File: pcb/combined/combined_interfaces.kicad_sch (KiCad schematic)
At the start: 19 parts, among them J5 CAN BUS, J6 FLOW HALL, J8 BOILER SSR, Q5 AO3401A, Q6 2N7002, U4 TJA1051T/3, U5 TMP102AIDRLR

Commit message: Draw the combined v2 schematic: 24 V buck and isolated gear pump interface
The pump dimmer and the zero-cross detector leave the board; the 230 V
valve channel stays. J7 brings 24 V from the pump supply to an
LMR33630A buck (5.02 V, enable at 18.4 V, off at 16.9 V), and J1 now sends
5 V to the screen. Two EL817C keep the pump's signal wires on their
isolated side: U8 turns the 1 kHz PWM on GPIO1 into a filtered setpoint
from the pump's own 5 V, U9 brings the tachometer back to GPIO3. DIM and
ZC become PUMP_SPEED and PUMP_TACHO.

The XIAO 5V pin is its USB VBUS with no diode; no diode is added either,
so USB is never plugged in with the XIAO on the board. New parts take new
references, so that no low-voltage net inherits a stale Mains netclass
pattern; those patterns and the pump and zero-cross DRC rules are gone.

F1 drops to 0.5 A, now that it protects the valve alone, and the AC
tracks to 1 mm. J3 is reversed so that its N faces N on J2. The HT396R
outline follows the Kefa drawing, and J8 becomes an HT396V header whose
screw plug takes the 0.75 mm² wires to the boiler SSR.

The board has been updated from the schematic; placement and routing are
still in progress.

Co-Authored-By: Claude Opus 5.5 <noreply@anthropic.com>
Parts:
- J8: footprint Connector_JST:JST_XH_B2B-XH-A_1x02_P2.50mm_Vertical -> Combined_Local:CONN-TH_P3.96_HT396V-3.96-2P; LCSC C158012 -> C577788; MPN B2B-XH-A(LF)(SN) -> HT396V-3.96-2P
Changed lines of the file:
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@@
 			)
 		)
-		(property "Footprint" "Connector_JST:JST_XH_B2B-XH-A_1x02_P2.50mm_Vertical"
+		(property "Footprint" "Combined_Local:CONN-TH_P3.96_HT396V-3.96-2P"
 			(at 288.29 242.57 0)
 			(hide yes)
@@
 			)
 		)
-		(property "Description" "Generic connector, single row, 01x02, script generated (kicad-library-utils/schlib/autogen/connector/)"
+		(property "Description" "Kefa HT396V vertical header; mating plug HT396K-3.96-2P (C577777, screw, up to 1.5 mm2) takes the 0.75 mm2 wires to the boiler SSR: 1 SSR (-), 2 SSR (+)"
 			(at 288.29 242.57 0)
 			(hide yes)
@@
 			)
 		)
-		(property "MPN" "B2B-XH-A(LF)(SN)"
+		(property "MPN" "HT396V-3.96-2P"
 			(at 288.29 242.57 0)
 			(hide yes)
@@
 			)
 		)
-		(property "LCSC" "C158012"
+		(property "LCSC" "C577788"
 			(at 288.29 242.57 0)
 			(hide yes)

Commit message: Move combined to basic passives, M2 holes and an HT3.96 flow connector
- Mounting holes H1 to H6 become M2 (2.2 mm NPTH) and move on the board;
  the AC wing narrows to 35 mm.
- Nine extended passives become JLCPCB basic parts: R3 150, R5/R6
  300 + 300, R7 100 (1206 kept: an 0805 breaks the 1.5 mm L-side
  clearance), FB divider 120k/30k (5.00 V), EN divider 330k/24k
  (18.2 V / 16.7 V), C1 10 uF 1206, C5 220 nF 0805, setpoint filter
  1.5k / 2.2 uF. Only C2 (10 nF 1 kV) stays extended.
- J6 (flow) becomes a Kefa HT396V-3.96-3P: the Digmesa 0.5 mm2 wires
  screw into the plug without the JST-SM to XH adapter. Footprint and
  3D model from LCSC, checked against the Kefa drawing.
- The MPB003 manufacturer datasheet replaces gearpump.pdf; it confirms
  the 7-wire pinout used on J9.

Co-Authored-By: Claude Opus 5.5 <noreply@anthropic.com>
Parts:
- J6: footprint Connector_JST:JST_XH_B3B-XH-A_1x03_P2.50mm_Vertical -> Combined_Local:CONN-TH_P3.96_HT396V-3.96-3P; LCSC C144394 -> C577789; MPN B3B-XH-A(LF)(SN) -> HT396V-3.96-3P; Note (none) -> Kefa HT396V vertical header; mating plug HT396K-3.96-3P (C5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
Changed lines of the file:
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@@
 			)
 		)
-		(property "Footprint" "Connector_JST:JST_XH_B3B-XH-A_1x03_P2.50mm_Vertical"
+		(property "Footprint" "Combined_Local:CONN-TH_P3.96_HT396V-3.96-3P"
 			(at 48.26 176.53 0)
 			(hide yes)
@@
 			)
 		)
-		(property "Description" "Generic connector, single row, 01x03, script generated (kicad-library-utils/schlib/autogen/connector/)"
+		(property "Description" ""
 			(at 48.26 176.53 0)
 			(hide yes)
@@
 			)
 		)
-		(property "MPN" "B3B-XH-A(LF)(SN)"
+		(property "MPN" "HT396V-3.96-3P"
 			(at 48.26 176.53 0)
 			(hide yes)
@@
 			)
 		)
-		(property "LCSC" "C144394"
+		(property "LCSC" "C577789"
 			(at 48.26 176.53 0)
 			(hide yes)
@@
 				)
 			)
+		)
+		(property "Note" "Kefa HT396V vertical header; mating plug HT396K-3.96-3P (C577778, screw) takes the 0.5 mm2 wires of the Digmesa cable: 1 GND, 2 +5V, 3 FLOW_PULSE"
+			(at 48.26 176.53 0)
+			(hide yes)
+			(show_name no)
+			(do_not_autoplace no)
+			(effects
+				(font
+					(size 1.27 1.27)
+				)
+			)

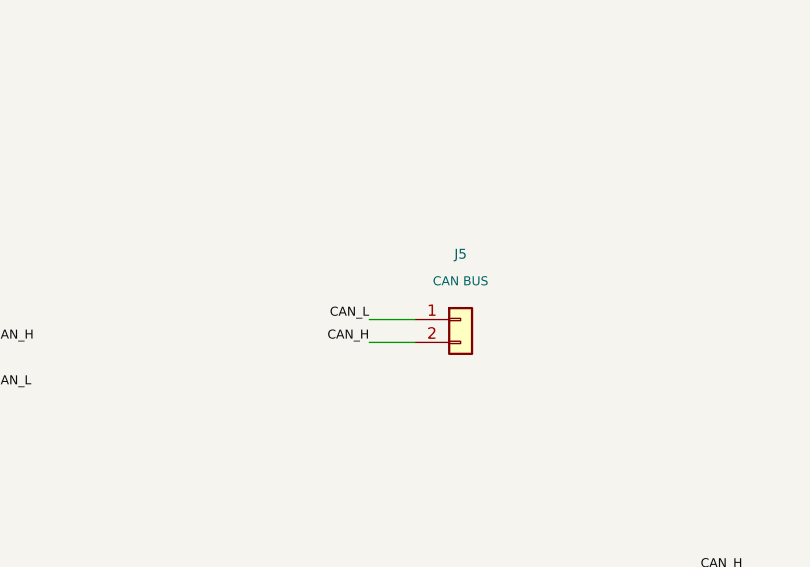
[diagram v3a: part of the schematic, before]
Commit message: Merge the combined screen 5 V and CAN connectors into one XH 4
J1 (5 V) and J5 (CAN) fed the same cable to the screen. One B4B-XH-A,
the part of J9, now carries 1 GND, 2 +5V, 3 CAN_L, 4 CAN_H and drops
C158012 from the extended parts. J1 takes the J9 placement corrections.

Co-Authored-By: Claude Opus 5.5 <noreply@anthropic.com>
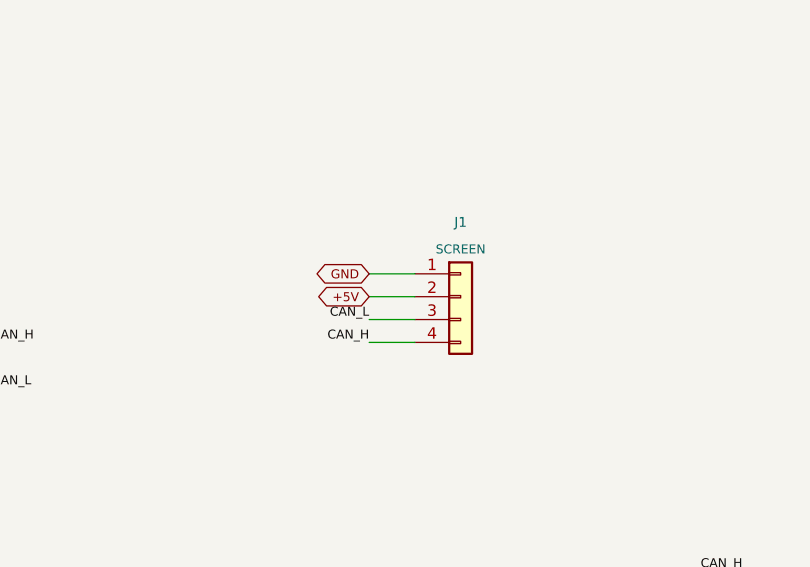
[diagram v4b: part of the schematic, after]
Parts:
- J1: renamed from J5; value CAN BUS -> SCREEN; footprint Connector_JST:JST_XH_B2B-XH-A_1x02_P2.50mm_Vertical -> Connector_JST:JST_XH_B4B-XH-A_1x04_P2.50mm_Vertical; symbol Connector_Generic:Conn_01x02 -> Connector_Generic:Conn_01x04; LCSC C158012 -> C144395; MPN B2B-XH-A(LF)(SN) -> B4B-XH-A(LF)(SN)
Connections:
- net +5V: now also J1.2 (Pin_2)
- net CAN_H: now also J1.4 (Pin_4); no longer J1.2 (Pin_2)
- net CAN_L: now also J1.3 (Pin_3); no longer J1.1 (Pin_1)
- net GND: now also J1.1 (Pin_1)
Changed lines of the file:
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@@
+		)
+	)
+	(wire
+		(pts
+			(xy 149.86 44.45) (xy 144.78 44.45)
+		)
+		(stroke
+			(width 0)
+			(type default)
+		)
+	)
+	(wire
+		(pts
+			(xy 149.86 46.99) (xy 144.78 46.99)
+		)
+		(stroke
+			(width 0)
+			(type default)
+		)
+	)
+	(global_label "GND"
+		(shape bidirectional)
+		(at 144.78 44.45 180)
+		(effects
+			(font
+				(size 1 1)
+			)
+			(justify right)
+		)
+		(property "Intersheetrefs" "${INTERSHEET_REFS}"
+			(at 144.78 44.45 180)
+			(hide yes)
+			(show_name no)
+			(do_not_autoplace no)
+			(effects
+				(font
+					(size 1 1)
+				)
+			)
+		)
+	)
+	(global_label "+5V"
+		(shape bidirectional)
+		(at 144.78 46.99 180)
+		(effects
+			(font
+				(size 1 1)
+			)
+			(justify right)
+		)
+		(property "Intersheetrefs" "${INTERSHEET_REFS}"
+			(at 144.78 46.99 180)
+			(hide yes)
+			(show_name no)
+			(do_not_autoplace no)
+			(effects
+				(font
+					(size 1 1)
+				)
+			)
 		)
 	)
@@
 	)
 	(symbol
-		(lib_id "Connector_Generic:Conn_01x02")
-		(at 154.94 49.53 0)
+		(lib_id "Connector_Generic:Conn_01x04")
+		(at 154.94 46.99 0)
 		(unit 1)
 		(body_style 1)
@@
 		(in_pos_files yes)
 		(dnp no)
-		(property "Reference" "J5"
-			(at 154.94 42.26 0)
+		(property "Reference" "J1"
+			(at 154.94 38.72 0)
 			(show_name no)
 			(do_not_autoplace no)
@@
 			)
 		)
-		(property "Value" "CAN BUS"
-			(at 154.94 45.26 0)
-			(show_name no)
-			(do_not_autoplace no)
-			(effects
-				(font
-					(size 1 1)
-				)
-			)
-		)
-		(property "Footprint" "Connector_JST:JST_XH_B2B-XH-A_1x02_P2.50mm_Vertical"
-			(at 154.94 49.53 0)
+		(property "Value" "SCREEN"
+			(at 154.94 41.72 0)
+			(show_name no)
+			(do_not_autoplace no)
+			(effects
+				(font
+					(size 1 1)
+				)
+			)
+		)
+		(property "Footprint" "Connector_JST:JST_XH_B4B-XH-A_1x04_P2.50mm_Vertical"
+			(at 154.94 46.99 0)
 			(hide yes)
 			(show_name no)
@@
 		)
 		(property "Datasheet" ""
-			(at 154.94 49.53 0)
-			(hide yes)
-			(show_name no)
-			(do_not_autoplace no)
-			(effects
-				(font
-					(size 1 1)
-				)
-			)
-		)
-		(property "Description" "Generic connector, single row, 01x02, script generated (kicad-library-utils/schlib/autogen/connector/)"
-			(at 154.94 49.53 0)
-			(hide yes)
-			(show_name no)
-			(do_not_autoplace no)
-			(effects
-				(font
-					(size 1 1)
-				)
-			)
-		)
-		(property "MPN" "B2B-XH-A(LF)(SN)"
-			(at 154.94 49.53 0)
-			(hide yes)
-			(show_name no)
-			(do_not_autoplace no)
-			(effects
-				(font
-					(size 1 1)
-				)
-			)
-		)
-		(property "LCSC" "C158012"
-			(at 154.94 49.53 0)
+			(at 154.94 46.99 0)
+			(hide yes)
+			(show_name no)
+			(do_not_autoplace no)
+			(effects
+				(font
+					(size 1 1)
+				)
+			)
+		)
+		(property "Description" "5 V and CAN to the screen, one cable: 1 GND, 2 +5V, 3 CAN_L, 4 CAN_H"
+			(at 154.94 46.99 0)
+			(hide yes)
+			(show_name no)
+			(do_not_autoplace no)
+			(effects
+				(font
+					(size 1 1)
+				)
+			)
+		)
+		(property "MPN" "B4B-XH-A(LF)(SN)"
+			(at 154.94 46.99 0)
+			(hide yes)
+			(show_name no)
+			(do_not_autoplace no)
+			(effects
+				(font
+					(size 1 1)
+				)
+			)
+		)
+		(property "LCSC" "C144395"
+			(at 154.94 46.99 0)
 			(hide yes)
 			(show_name no)
@@
 		)
 		(pin "2"
+		)
+		(pin "3"
+		)
+		(pin "4"
 		)
 		(instances
 			(project "combined"
 				(path "/a3ee807d-f8aa-4db3-ad94-73a886b6ed37/75feafe7-4600-5614-9e51-33ca428cd046"
-					(reference "J5")
+					(reference "J1")
 					(unit 1)
 				)
